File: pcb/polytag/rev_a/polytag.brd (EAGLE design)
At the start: 46.2 x 40 mm, 46 parts, among them J1 TC2030-JLINK-NL, J2 TC2030-JLINK-NL, J3 MICRO_USB_B_HIROSE_ZX62-B-5PA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, J4 BAT_HOLE, J5 BAT_HOLE, U1 NRF51822QF, U2 TRIPOINT, U3 LTC4065, U4 TPS715AXX, X1 EPSON-FA-128

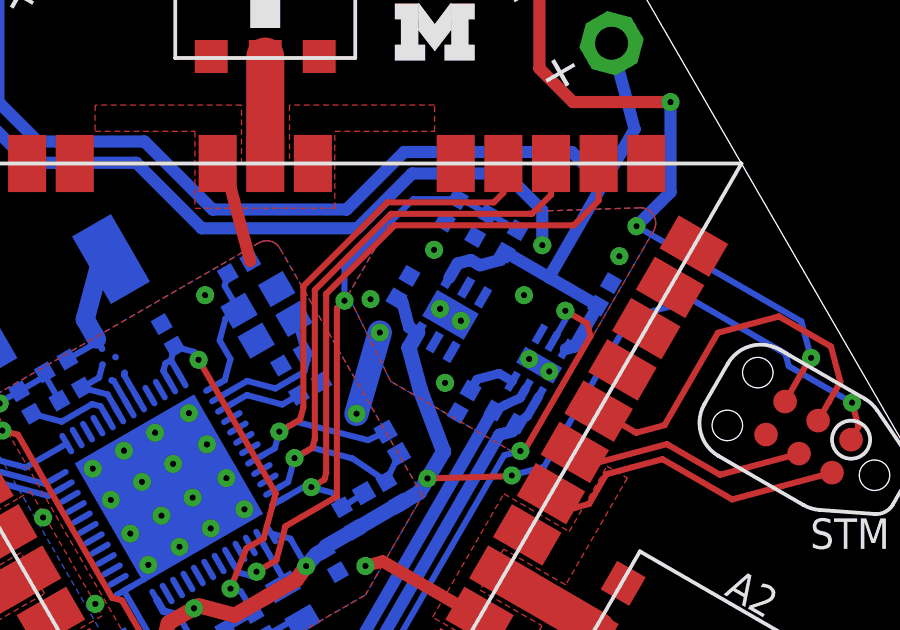
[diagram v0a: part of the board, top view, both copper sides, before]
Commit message: fixed tenting problem
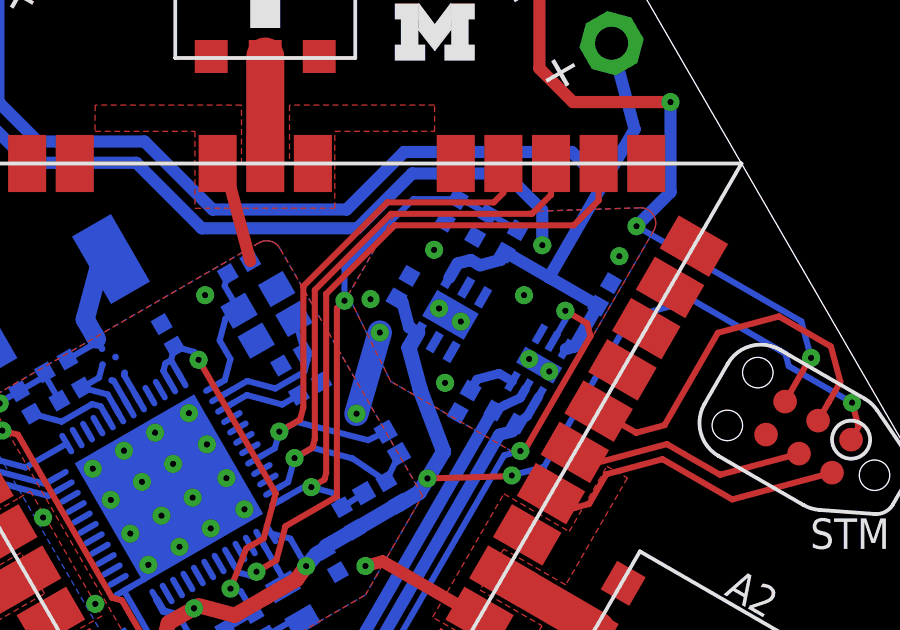
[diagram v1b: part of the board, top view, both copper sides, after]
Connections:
- net GND: no longer U4.TP, U4.TP2
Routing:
- net GND: vias 36 -> 38
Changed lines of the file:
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@@
 <contactref element="U4" pad="TP3"/>
 <contactref element="U4" pad="2"/>
-<contactref element="U4" pad="TP"/>
-<contactref element="U4" pad="TP2"/>
 <contactref element="U4" pad="3"/>
 <contactref element="U4" pad="4"/>
@@
 <via x="-2.00305625" y="4.781821875" extent="1-16" drill="0.2032"/>
 <contactref element="TP4" pad="TP"/>
+<via x="5.793075" y="4.3404" extent="1-16" drill="0.2032"/>
+<via x="6.519540625" y="3.901671875" extent="1-16" drill="0.2032"/>
 </signal>
 <signal name="VCC">
